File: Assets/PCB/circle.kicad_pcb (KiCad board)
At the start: 2 copper layers, 40.6 x 40.6 mm, 24 parts

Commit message: Update circle.kicad_pcb
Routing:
- net (no net): track 793.3 -> 795.3 mm
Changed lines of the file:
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@@
   (segment (start 127.254 87.884) (end 131.064 87.884) (width 0.25) (layer "B.Cu") (net 0))
   (segment (start 124.968 104.648) (end 120.65 100.33) (width 0.25) (layer "B.Cu") (net 0))
+  (segment (start 120.904 114.3) (end 120.142 114.3) (width 0.25) (layer "B.Cu") (net 0))
   (segment (start 132.08 100.33) (end 136.144 100.33) (width 0.25) (layer "B.Cu") (net 0))
   (segment (start 108.712 96.774) (end 108.712 93.98) (width 0) (layer "B.Cu") (net 0))
@@
   (segment (start 124.714 83.058) (end 120.65 83.058) (width 0) (layer "B.Cu") (net 0))
   (segment (start 108.712 97.774) (end 110.728 97.774) (width 0.25) (layer "B.Cu") (net 0))
+  (segment (start 121.158 114.3) (end 120.904 114.3) (width 0.25) (layer "B.Cu") (net 0))
   (segment (start 111.633 90.805) (end 114.935 90.805) (width 0.25) (layer "B.Cu") (net 0))
   (segment (start 119.126 110.49) (end 117.602 110.49) (width 0.25) (layer "B.Cu") (net 0))
@@
   (segment (start 123.952 88.9) (end 120.396 88.9) (width 0.25) (layer "B.Cu") (net 0))
   (segment (start 122.174 115.57) (end 122.174 114.3) (width 0.25) (layer "B.Cu") (net 0))
+  (segment (start 122.174 114.3) (end 121.158 114.3) (width 0.25) (layer "B.Cu") (net 0))
   (segment (start 116.332 118.364) (end 113.03 115.062) (width 0.25) (layer "B.Cu") (net 0))
   (zone (net 0) (net_name "") (layer "B.Cu") (hatch edge 0.5)

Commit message: Update circle.kicad_pcb
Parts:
- removed the REF** at (127.3, 82.8)
- removed VS: PinHeader_1x02_P1.00mm_Vertical, Connector_PinHeader_1.00mm:PinHeader_1x02_P1.00mm_Vertical
- added SIG: SolderJumper-2_P1.3mm_Bridged2Bar_Pad1.0x1.5mm, Jumper:SolderJumper-2_P1.3mm_Bridged2Bar_Pad1.0x1.5mm, F.Cu at (127.3, 82.8)
- added VIB: PinHeader_1x02_P2.54mm_Vertical, Connector_PinHeader_2.54mm:PinHeader_1x02_P2.54mm_Vertical, F.Cu at (108.7, 97.8)
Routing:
- net (no net): track 795.3 -> 793.5 mm, vias 4 -> 19
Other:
- board text added: "Tactile Sensor PressTip V2.1"
- board text removed: "Tactile Sensor PressTip"

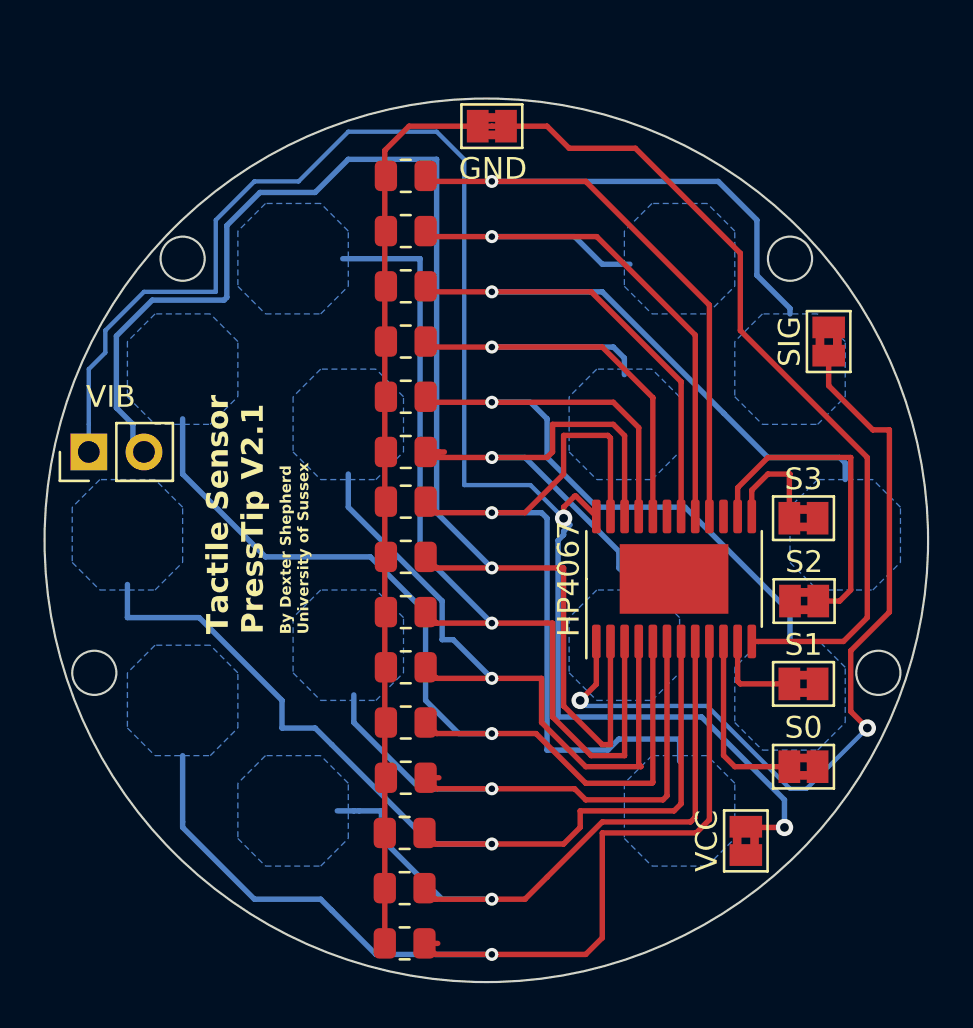
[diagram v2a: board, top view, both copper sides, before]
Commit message: updated PCBs for one layer
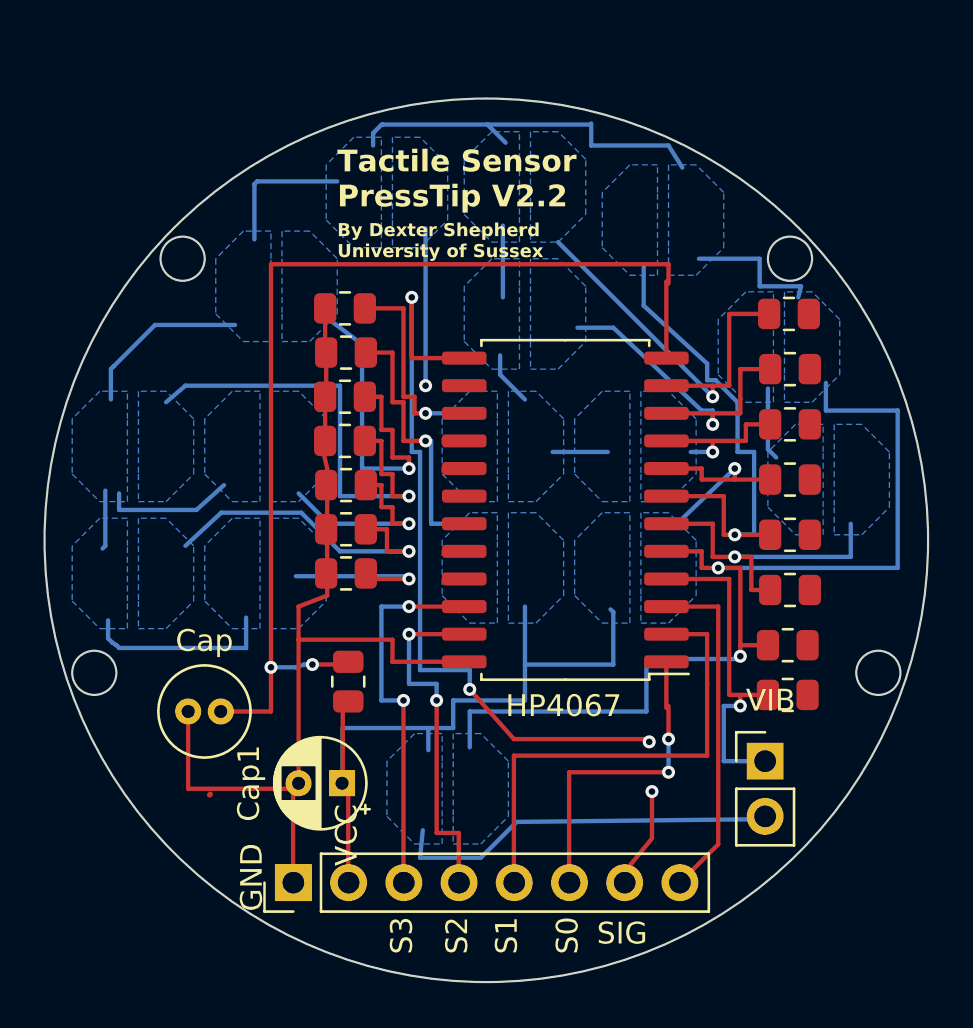
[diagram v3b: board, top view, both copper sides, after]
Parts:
- removed S0, S1, S2, S3, SIG (x2), VCC: SolderJumper-2_P1.3mm_Bridged2Bar_Pad1.0x1.5mm, Jumper:SolderJumper-2_P1.3mm_Bridged2Bar_Pad1.0x1.5mm
- added Cap: C_Radial_D4.0mm_H5.0mm_P1.50mm, Capacitor_THT:C_Radial_D4.0mm_H5.0mm_P1.50mm, F.Cu at (113.3, 109.7)
- added Cap1: CP_Radial_D4.0mm_P2.00mm, Capacitor_THT:CP_Radial_D4.0mm_P2.00mm, F.Cu at (120.4, 113.0)
- added GPIO: PinHeader_1x08_P2.54mm_Vertical, Connector_PinHeader_2.54mm:PinHeader_1x08_P2.54mm_Vertical, F.Cu at (118.1, 117.6)
- added RP: R_0805_2012Metric, Resistor_SMD:R_0805_2012Metric, F.Cu at (120.7, 108.4)
- HP4067: value HTSSOP-24-1EP_4.4x7.8mm_P0.65mm_EP3.2x5mm -> SOIC-24W_7.5x15.4mm_P1.27mm; footprint Package_SO:HTSSOP-24-1EP_4.4x7.8mm_P0.65mm_EP3.2x5mm -> Package_SO:SOIC-24W_7.5x15.4mm_P1.27mm
- moved VIB 34.2 mm to (139.8, 112.0), turned to 0 degrees
- moved j10 24.1 mm to (141.0, 104.1), turned to 0 degrees
- moved j11 24.1 mm to (141.0, 101.6), turned to 0 degrees
- moved j12 24.1 mm to (141.0, 99.1), turned to 0 degrees
- moved j13 24.0 mm to (141.0, 96.5), turned to 0 degrees
- moved j14 24.0 mm to (141.0, 94.0), turned to 0 degrees
- moved j15 22.3 mm to (140.9, 91.4), turned to 0 degrees
- moved j9 18.0 mm to (140.9, 106.7), turned to 0 degrees
- moved j8 17.6 mm to (140.9, 109.0), turned to 0 degrees
- moved j7 8.58 mm to (120.5, 103.4), turned to 0 degrees
- moved j4 6.71 mm to (120.5, 91.2), turned to 0 degrees
- moved j3 6.23 mm to (120.5, 93.2), turned to 0 degrees
- moved HP4067 5.92 mm to (130.6, 100.5), turned to 180 degrees
- moved j2 5.80 mm to (120.5, 95.2), turned to 0 degrees
- moved j5 5.36 mm to (120.5, 97.3), turned to 0 degrees
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- renumbered REF** to j1, REF** to j10, REF** to j11, REF** to j12, REF** to j13, REF** to j14, REF** to j15, REF** to j2, REF** to j3, REF** to j4, REF** to j5, REF** to j6, REF** to j7, REF** to j8, REF** to j9
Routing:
- net (no net): track 793.5 -> 97.7 mm, vias 19 -> 29
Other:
- board text added: "P0"
- board text added: "P1"
- board text added: "P10"
- board text added: "P11"
- board text added: "P13"
- board text added: "P14"
- board text added: "P15"
- board text added: "P2"
- board text added: "P3"
- board text added: "P4"
- board text added: "P5"
- board text added: "P6"
- board text added: "P7"
- board text added: "P8"
- board text added: "P9"
- board text added: "S0"
- board text added: "S1"
- board text added: "S2"
- board text added: "S3"
- board text added: "SIG"
- board text added: "Tactile Sensor PressTip V2.2"
- board text added: "VCC"
- board text added: "p12"
- board text removed: "Tactile Sensor PressTip V2.1"
